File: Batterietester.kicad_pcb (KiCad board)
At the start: 2 copper layers, 15 parts, among them J1 Load, J2 Power, SW1 SW_Push, SW2 SW_Push, U1 LM3914

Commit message: Board design
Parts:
- added REF***: KiCad-Logo2_8mm_SilkScreen, Symbols:KiCad-Logo2_8mm_SilkScreen, F.Cu at (148.6, 114.9)
- added REF***: OSHW-Logo2_9.8x8mm_SilkScreen, Symbols:OSHW-Logo2_9.8x8mm_SilkScreen, F.Cu at (130.2, 115.6)
- J1, J2: footprint Pin_Headers:Pin_Header_Straight_1x02_Pitch2.54mm -> Pin_Headers:Pin_Header_Angled_1x02_Pitch2.54mm
- moved SW1 20.5 mm to (154.9, 96.5)
- moved SW2 19.6 mm to (154.9, 88.3)
- moved J1 18.1 mm to (137.2, 82.5), turned to 90 degrees
- moved R4 18.0 mm to (131.4, 98.4)
- moved RV1 14.9 mm to (145.4, 109.2)
- moved RV2 14.1 mm to (145.4, 99.1)
- moved R1 10.9 mm to (142.2, 90.2), turned to 180 degrees
- moved R3 7.65 mm to (116.2, 76.2)
- moved J2 6.02 mm to (149.9, 82.5), turned to 90 degrees
- moved U1 3.59 mm to (119.4, 90.2)
- moved BAR1 3.59 mm to (104.1, 87.6)
- moved C1 3.24 mm to (118.7, 81.9), turned to 270 degrees
- moved D1 3.18 mm to (108.6, 79.4), turned to 90 degrees
- moved R5 2.62 mm to (131.4, 108.6)
- moved R2 2.54 mm to (131.4, 103.5)
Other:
- board outline added: 66 x 52.7 mm
- board text added: "Battery tester"
- board text added: "Empty"
- board text added: "Full"
- board text added: "Load 12R"
- board text added: "Power"
- board text added: "Test"
- board text added: "https://github.com/aboettger/battery-tester"
- board text removed: "Load"

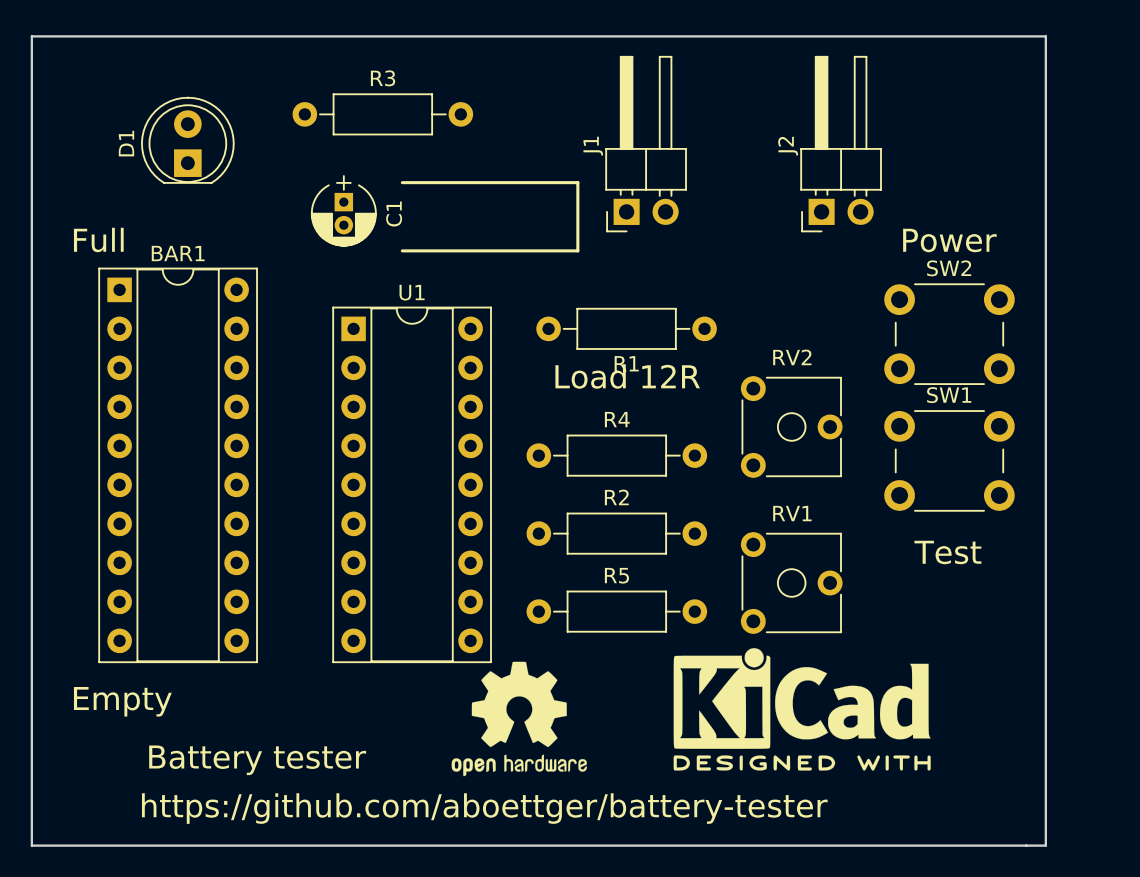
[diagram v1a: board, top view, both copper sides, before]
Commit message: added Filled zones
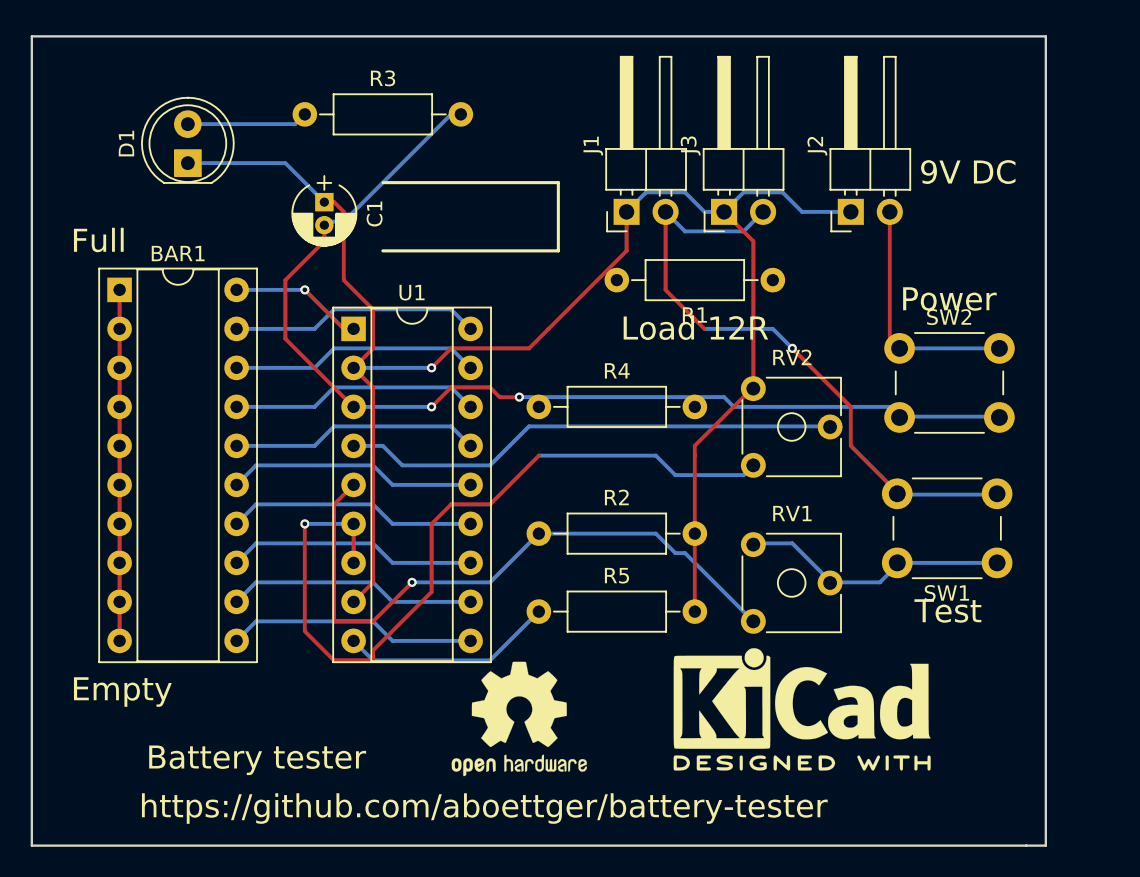
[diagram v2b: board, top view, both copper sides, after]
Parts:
- added J3: Load, Pin_Headers:Pin_Header_Angled_1x02_Pitch2.54mm, F.Cu at (143.5, 82.5)
- moved SW1 10.9 mm to (161.3, 105.4), turned to 180 degrees
- moved R1 5.46 mm to (146.7, 87.0)
- moved R4 3.17 mm to (131.4, 95.2)
- moved SW2 3.17 mm to (154.9, 91.4)
- moved J2 1.90 mm to (151.8, 82.5)
- moved C1 1.27 mm to (117.5, 81.9)
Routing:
- net GND: track 0.00 -> 108.0 mm, vias 0 -> 1
- net VCC: track 0.00 -> 70.2 mm, vias 0 -> 2
- net Net-(R4-Pad1): track 0.00 -> 52.0 mm, vias 0 -> 1
- net SW_L: track 0.00 -> 41.5 mm, vias 0 -> 1
- net Net-(R2-Pad1): track 0.00 -> 41.5 mm, vias 0 -> 1
- net Net-(RV2-Pad2): track 0.00 -> 32.8 mm
- net Net-(BAR1-Pad1): track 0.00 -> 22.9 mm
- net Sig: track 0.00 -> 18.0 mm
- net Net-(BAR1-Pad16): track 0.00 -> 16.3 mm
- net Net-(BAR1-Pad14): track 0.00 -> 16.3 mm
- net Net-(BAR1-Pad19): track 0.00 -> 16.3 mm
- net Net-(BAR1-Pad18): track 0.00 -> 16.3 mm
- net Net-(BAR1-Pad17): track 0.00 -> 16.3 mm
- net Net-(BAR1-Pad15): track 0.00 -> 16.3 mm
- net Net-(BAR1-Pad13): track 0.00 -> 16.3 mm
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- added copper zone on B.Cu, net GND
- added copper zone on F.Cu, net GND
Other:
- board text added: "9V DC"

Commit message: corrected orientation
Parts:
- moved BAR1 25.1 mm to (111.1, 111.8), turned to 180 degrees
- moved U1 21.1 mm to (125.1, 110.5), turned to 180 degrees
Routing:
- net Net-(R4-Pad1): track 52.0 -> 24.4 mm, vias 1 -> 0
- net Net-(R2-Pad1): track 41.5 -> 24.0 mm, vias 1 -> 0
- net Net-(BAR1-Pad20): track 8.67 -> 23.2 mm, vias 1 -> 0
- net VCC: track 70.2 -> 82.4 mm
- net Net-(R5-Pad1): track 13.9 -> 21.0 mm
- net SW_L: track 41.5 -> 36.2 mm, vias 1 -> 0
- net GND: track 108.0 -> 103.9 mm, vias 1 -> 0
- net Net-(BAR1-Pad16): track 16.3 -> 14.5 mm
- net Net-(BAR1-Pad14): track 16.3 -> 14.5 mm
- net Net-(BAR1-Pad19): track 16.3 -> 14.5 mm
- net Net-(BAR1-Pad18): track 16.3 -> 14.5 mm
- net Net-(BAR1-Pad17): track 16.3 -> 14.5 mm
- net Net-(BAR1-Pad15): track 16.3 -> 14.5 mm
- net Net-(BAR1-Pad13): track 16.3 -> 14.5 mm
- net Net-(BAR1-Pad12): track 16.3 -> 14.5 mm
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
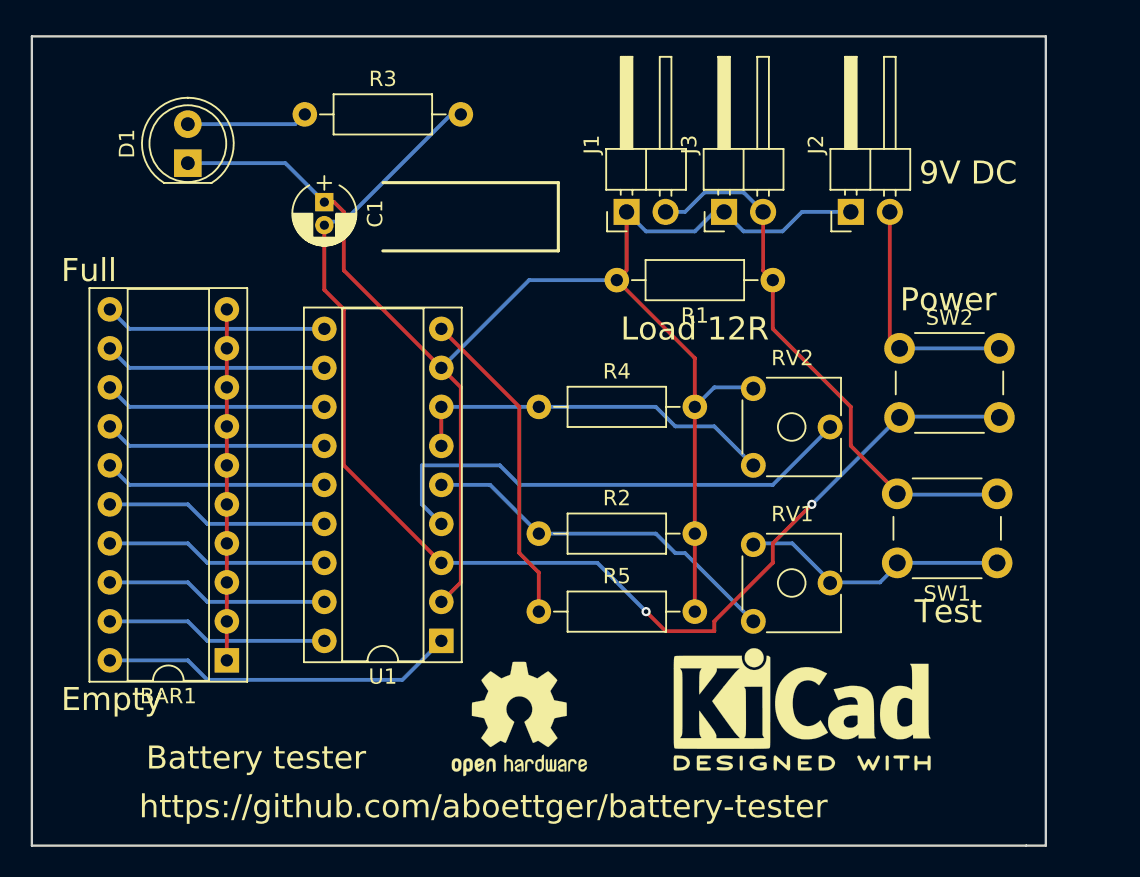
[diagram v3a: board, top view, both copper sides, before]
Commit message: added mounting holes added mode jumper
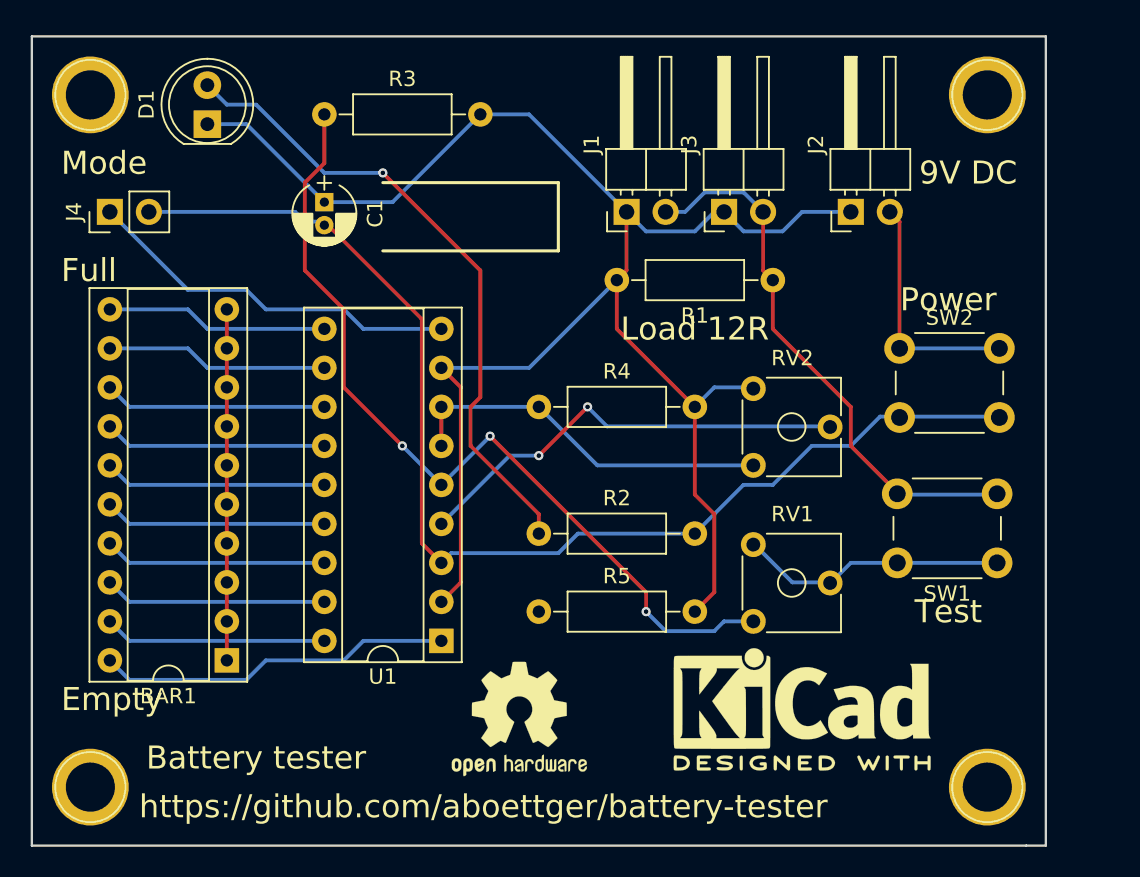
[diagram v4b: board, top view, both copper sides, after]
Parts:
- added J4: CONN_01X02, Pin_Headers:Pin_Header_Straight_1x02_Pitch2.54mm, F.Cu at (103.5, 82.5)
- added REF**: 1pin, Connect:1pin, F.Cu at (102.2, 120.0)
- added REF**: 1pin, Connect:1pin, F.Cu at (160.7, 120.0)
- added REF**: 1pin, Connect:1pin, F.Cu at (160.7, 74.9)
- added REF**: 1pin, Connect:1pin, F.Cu at (102.2, 74.9)
- J1, J3: value Load -> CONN_01X02
- J2: value Power -> CONN_01X02
- R2: value 10k -> 680
- R3: value 680 -> 10k
- moved D1 2.84 mm to (109.9, 76.8)
- moved R3 1.27 mm to (117.5, 76.2)
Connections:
- C1 pad 2: VCC -> 9V
- R2 pad 1: Net-(R2-Pad1) -> Net-(D1-Pad2)
- R2 pad 2: GND -> 9V
- R3 pad 1: Net-(D1-Pad2) -> Net-(R3-Pad1)
- R3 pad 2: VCC -> GND
- R5 pad 1: Net-(R5-Pad1) -> (no net)
- RV1 pad 1: Net-(R2-Pad1) -> Net-(R3-Pad1)
- SW2 pad 2: VCC -> 9V
- U1 pad 3: VCC -> 9V
- U1 pad 5: Net-(R2-Pad1) -> Net-(R3-Pad1)
- U1 pad 9: Net-(R5-Pad1) -> Net-(J4-Pad1)
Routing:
- net VCC: track 82.4 -> 0.00 mm, vias 2 -> 0
- net 9V: track 0.00 -> 77.9 mm
- net Net-(R3-Pad1): track 0.00 -> 56.2 mm, vias 0 -> 3
- net Net-(D1-Pad2): track 7.88 -> 42.0 mm, vias 0 -> 1
- net Net-(J4-Pad1): track 0.00 -> 24.7 mm
- net Net-(R2-Pad1): track 24.0 -> 0.00 mm
- net Net-(R5-Pad1): track 21.0 -> 0.00 mm
- net GND: track 103.9 -> 115.1 mm
- net Net-(RV2-Pad2): track 33.2 -> 29.2 mm, vias 0 -> 2
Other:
- board text added: "Mode"

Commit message: corrected LED bar connection
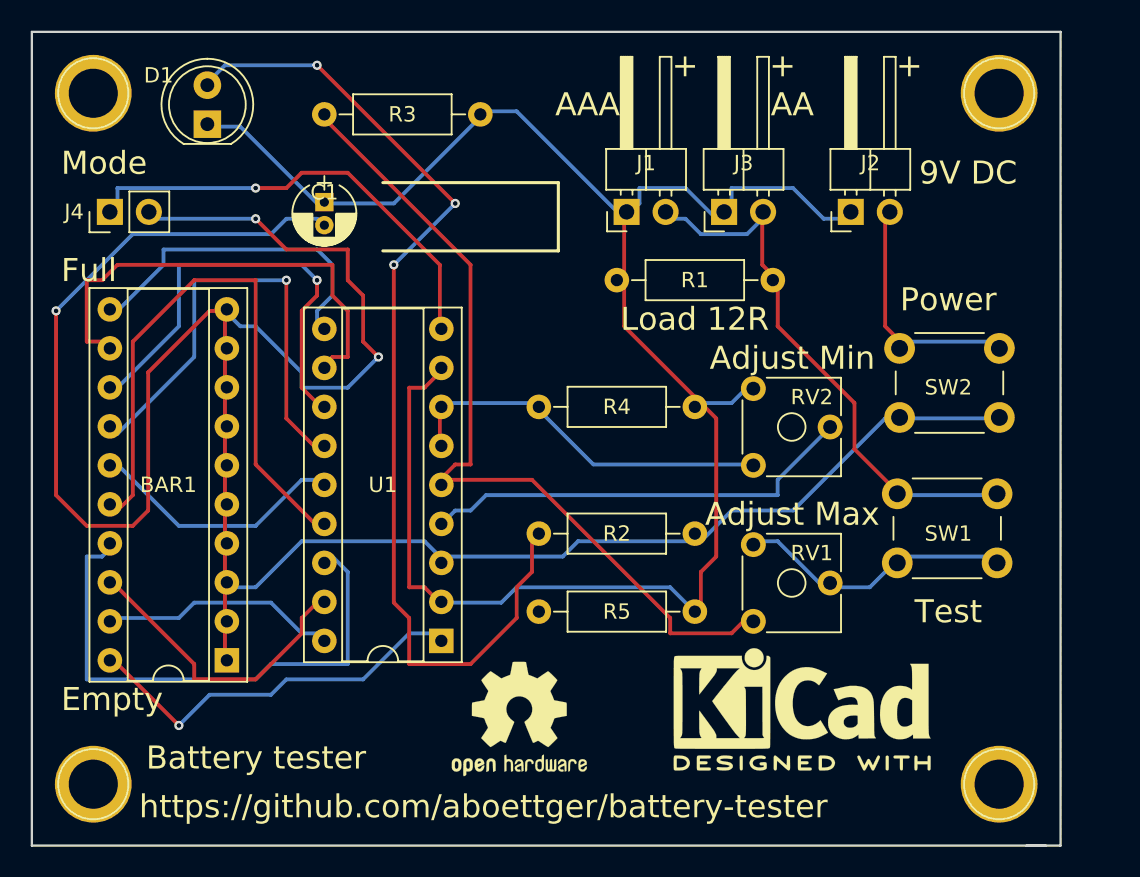
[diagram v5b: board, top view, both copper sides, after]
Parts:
- moved REF** 0.79 mm to (161.4, 119.8)
- moved REF** 0.78 mm to (161.4, 74.8)
- moved REF** 0.27 mm to (102.4, 119.8)
- moved REF** 0.22 mm to (102.4, 74.8)
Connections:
- BAR1 pad 1: Net-(BAR1-Pad1) -> 9V
- BAR1 pad 10: Net-(BAR1-Pad1) -> 9V
- BAR1 pad 2: Net-(BAR1-Pad1) -> 9V
- BAR1 pad 3: Net-(BAR1-Pad1) -> 9V
- BAR1 pad 4: Net-(BAR1-Pad1) -> 9V
- BAR1 pad 5: Net-(BAR1-Pad1) -> 9V
- BAR1 pad 6: Net-(BAR1-Pad1) -> 9V
- BAR1 pad 7: Net-(BAR1-Pad1) -> 9V
- BAR1 pad 8: Net-(BAR1-Pad1) -> 9V
- BAR1 pad 9: Net-(BAR1-Pad1) -> 9V
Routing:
- net 9V: track 77.9 -> 177.7 mm, vias 0 -> 3
- net Net-(BAR1-Pad16): track 14.5 -> 39.9 mm
- net Net-(D1-Pad2): track 42.0 -> 66.9 mm, vias 1 -> 3
- net Net-(BAR1-Pad17): track 14.5 -> 37.4 mm
- net Net-(BAR1-Pad1): track 22.9 -> 0.00 mm
- net Net-(BAR1-Pad12): track 14.5 -> 32.5 mm
- net GND: track 115.1 -> 132.6 mm
- net Net-(BAR1-Pad14): track 14.5 -> 31.1 mm, vias 0 -> 1
- net Net-(BAR1-Pad13): track 14.5 -> 28.9 mm, vias 0 -> 1
- net Net-(BAR1-Pad11): track 14.5 -> 22.1 mm
- net Net-(J4-Pad1): track 24.7 -> 30.8 mm, vias 0 -> 1
- net Net-(BAR1-Pad18): track 14.5 -> 19.8 mm
- net Sig: track 17.7 -> 21.0 mm
- net Net-(BAR1-Pad20): track 23.2 -> 26.2 mm, vias 0 -> 1
- net Net-(BAR1-Pad15): track 14.5 -> 17.0 mm
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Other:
- board size 66 x 52.7 mm -> 67 x 53 mm
- rule pad_to_mask_clearance: 0.2 -> 0
- board text added: "+"
- board text added: "45 mm"
- board text added: "59 mm"
- board text added: "AA"
- board text added: "AAA"
- board text added: "Adjust Max"
- board text added: "Adjust Min"

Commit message: changed variable resistors
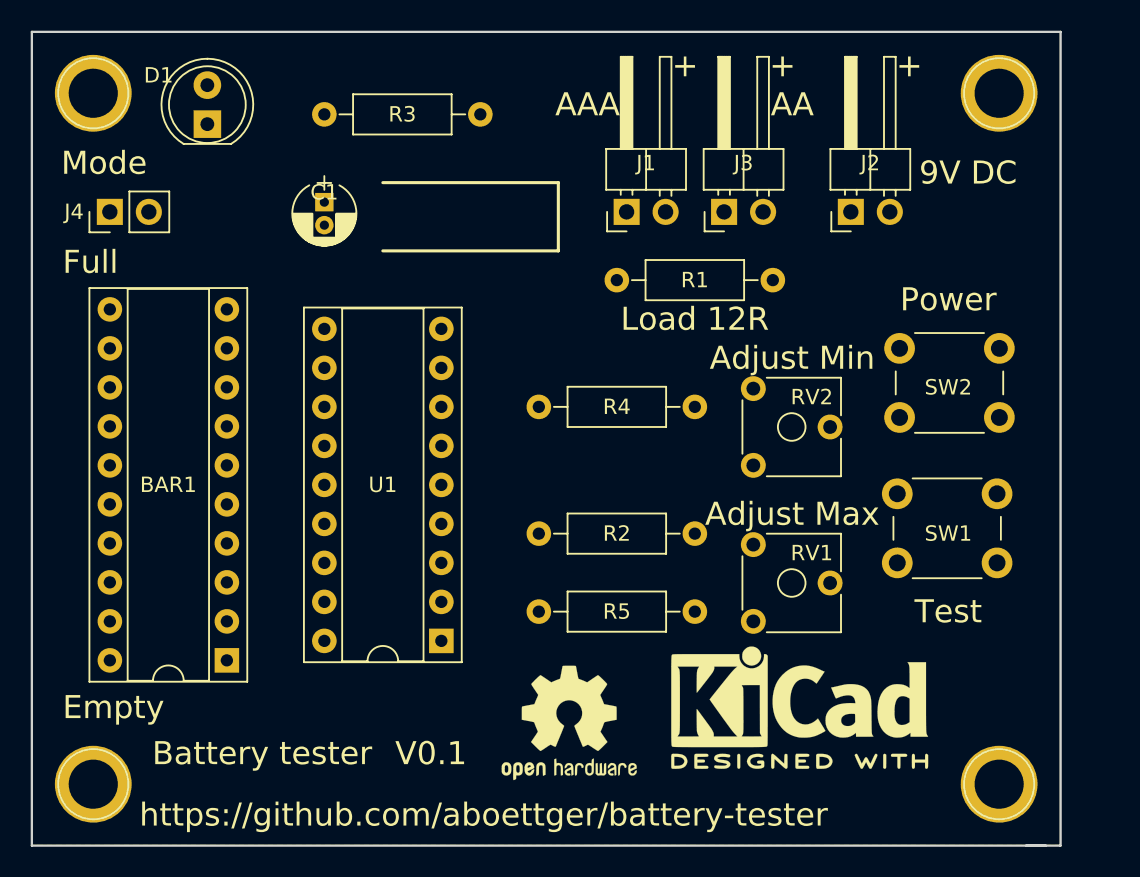
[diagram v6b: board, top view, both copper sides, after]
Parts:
- moved REF*** 3.26 mm to (133.4, 115.8)
- moved REF*** 0.20 mm to (148.4, 114.8)
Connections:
- net Net-(RV2-Pad2) renamed Pin4
- RV1 pad 1: Net-(R3-Pad1) -> Sig
- RV1 pad 3: Sig -> Net-(R3-Pad1)
- RV2 pad 1: Net-(R4-Pad1) -> GND
- RV2 pad 3: GND -> Net-(R4-Pad1)
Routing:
- net 9V: track 177.7 -> 0.00 mm, vias 3 -> 0
- net GND: track 132.6 -> 0.00 mm
- net Net-(D1-Pad2): track 66.9 -> 0.00 mm, vias 3 -> 0
- net Net-(R3-Pad1): track 56.4 -> 0.00 mm
- net Net-(BAR1-Pad16): track 39.9 -> 0.00 mm
- net SW_L: track 37.4 -> 0.00 mm
- net Net-(BAR1-Pad17): track 37.4 -> 0.00 mm
- net Net-(BAR1-Pad12): track 32.5 -> 0.00 mm
- net Net-(BAR1-Pad14): track 31.1 -> 0.00 mm, vias 1 -> 0
- net Net-(J4-Pad1): track 30.8 -> 0.00 mm, vias 1 -> 0
- net Net-(BAR1-Pad13): track 28.9 -> 0.00 mm, vias 1 -> 0
- net Pin4: track 28.8 -> 0.00 mm
- net Net-(R4-Pad1): track 26.9 -> 0.00 mm
- net Net-(BAR1-Pad20): track 26.2 -> 0.00 mm, vias 1 -> 0
- net Net-(BAR1-Pad11): track 22.1 -> 0.00 mm
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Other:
- board text added: "V0.1"

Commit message: added revision
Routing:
- net 9V: track 0.00 -> 179.9 mm, vias 0 -> 2
- net GND: track 0.00 -> 130.8 mm
- net Net-(R3-Pad1): track 0.00 -> 52.9 mm
- net Net-(D1-Pad2): track 0.00 -> 45.2 mm, vias 0 -> 1
- net SW_L: track 0.00 -> 37.4 mm
- net Net-(BAR1-Pad17): track 0.00 -> 37.4 mm
- net Net-(BAR1-Pad15): track 0.00 -> 33.8 mm
- net Net-(J4-Pad1): track 0.00 -> 30.8 mm, vias 0 -> 1
- net Net-(BAR1-Pad13): track 0.00 -> 30.3 mm, vias 0 -> 1
- net Net-(BAR1-Pad14): track 0.00 -> 29.9 mm
- net Net-(BAR1-Pad12): track 0.00 -> 29.3 mm
- net Pin4: track 0.00 -> 28.3 mm, vias 0 -> 1
- net Net-(BAR1-Pad20): track 0.00 -> 25.9 mm, vias 0 -> 1
- net Net-(R4-Pad1): track 0.00 -> 25.6 mm
- net Sig: track 0.00 -> 20.6 mm
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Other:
- board text added: "Rev 1"
- board text removed: "V0.1"

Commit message: finished Rev 1
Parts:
- moved R3 30.9 mm to (131.4, 103.8)
- moved R2 29.7 mm to (118.4, 76.8)
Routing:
- net Net-(D1-Pad2): track 45.2 -> 10.0 mm, vias 1 -> 0
- net Net-(R3-Pad1): track 52.9 -> 24.2 mm
- net 9V: track 179.9 -> 194.9 mm
- net Net-(BAR1-Pad15): track 33.8 -> 45.8 mm, vias 0 -> 2
- net Net-(BAR1-Pad18): track 19.8 -> 31.6 mm, vias 0 -> 1
- net Net-(BAR1-Pad14): track 29.9 -> 41.7 mm, vias 0 -> 1
- net Net-(BAR1-Pad17): track 37.4 -> 25.9 mm
- net GND: track 130.8 -> 121.4 mm
- net Net-(BAR1-Pad13): track 30.3 -> 23.8 mm, vias 1 -> 0
- net Net-(BAR1-Pad11): track 17.5 -> 16.1 mm
- net Net-(BAR1-Pad12): track 29.3 -> 27.9 mm
- net Net-(BAR1-Pad20): track 25.9 -> 27.0 mm, vias 1 -> 0
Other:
- board text added: "hole distance 45 mm"
- board text added: "hole distance 59 mm"
- board text removed: "45 mm"
- board text removed: "59 mm"
